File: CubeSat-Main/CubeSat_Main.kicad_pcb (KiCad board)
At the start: 2 copper layers, 92 x 92 mm, 22 parts, among them J1 Conn_01x03_Pin, J2 Conn_01x08_Socket, U1 STM32F411CEU6 - BlackPill, U2 LORA E220-900T22D, U3 BNO055, U4 GPS_NEO6M, U5 LM7805_TO220, U6 LM35-LP

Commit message: Mostly fine tuning the boards, also added capacitor for battery ADC
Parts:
- added C4: 0.1uF, Capacitor_THT:C_Disc_D8.0mm_W2.5mm_P5.00mm, F.Cu at (149.6, 98.3)
- added J3: Conn_01x03_Pin, Connector_PinHeader_2.54mm:PinHeader_1x03_P2.54mm_Vertical, F.Cu at (165.3, 97.0)
- C2, C3: footprint Capacitor_THT:C_Disc_D8.0mm_W5.0mm_P7.50mm -> Capacitor_THT:C_Disc_D8.0mm_W2.5mm_P5.00mm
- R6: value 100K -> 10K
- R7: value 47K -> 4.7K
- moved C3 6.77 mm to (120.6, 141.4), turned to 180 degrees
- moved C1 3.78 mm to (161.2, 93.2)
- moved R6 3.76 mm to (149.9, 91.1)
- moved R7 3.76 mm to (142.3, 94.8)
- moved U5 3.64 mm to (159.9, 98.1)
- moved C2 2.65 mm to (154.3, 103.8)
- moved U4 0.37 mm to (138.6, 70.6)
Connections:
- C3 pad 1: STM_3.3V -> GND
- C3 pad 2: GND -> VIN_5V2
- U1 pad 5V2: unconnected-(U1-5V-Pad5V2) -> VIN_5V2
- U2 pad 6: 5V_LDO -> 5V_E220
- U3 pad 1: STM_3.3V -> VIN_5V2
- U6 pad 1: 5V_LDO -> 5V_E220
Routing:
- net VIN_5V: track 44.8 -> 102.3 mm
- net STM_3.3V: track 77.8 -> 28.7 mm
- net 5V_E220: track 0.00 -> 45.2 mm
- net VIN_5V2: track 0.00 -> 41.7 mm
- net 5V_LDO: track 33.2 -> 20.8 mm
- net Vbat_ADC: track 8.87 -> 17.0 mm
- net GND: track 238.4 -> 240.7 mm
- net Net-(D2-K): track 4.14 -> 5.17 mm
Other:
- board text added: "-BNO055"
- board text added: "-GPS NEO6M"
- board text added: "-LoRa EBYTE 220"
- board text added: "-STM32F411CEU6"
- board text added: "BUCK"
- board text added: "LDO"
- board text added: "U2"

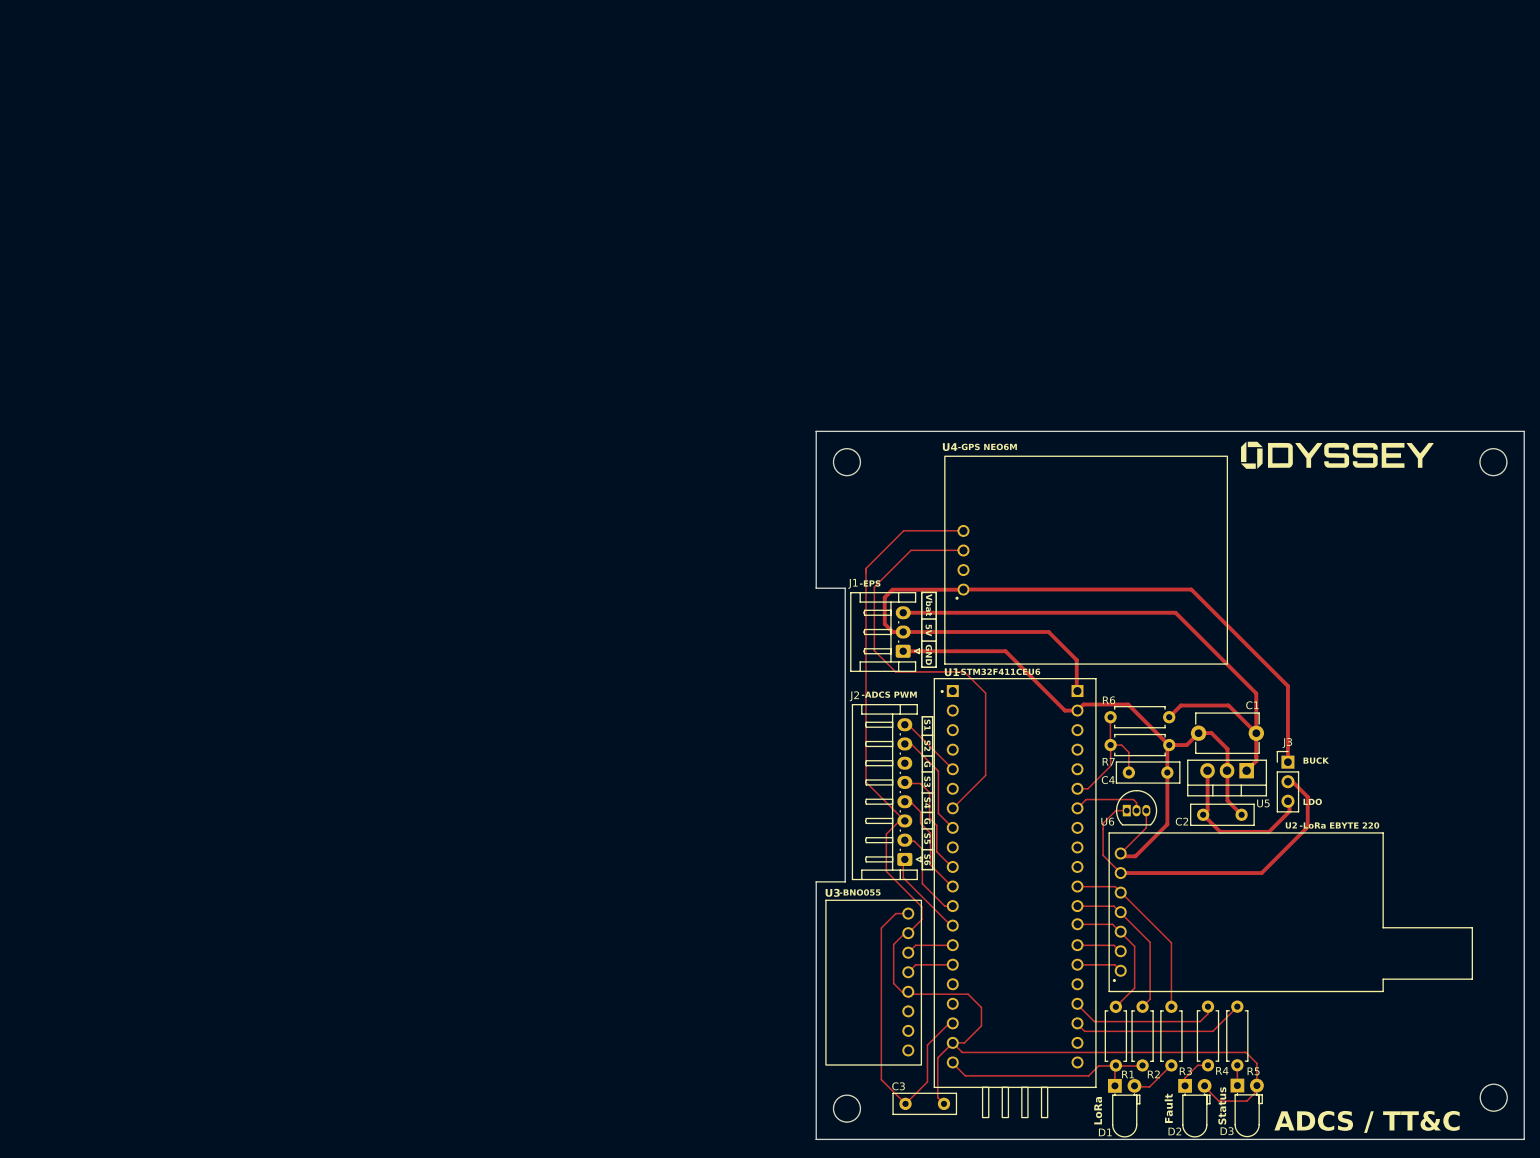
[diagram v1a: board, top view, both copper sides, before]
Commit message: Changing the size of all traces to fit the 1 mm requirement of the draft PCB
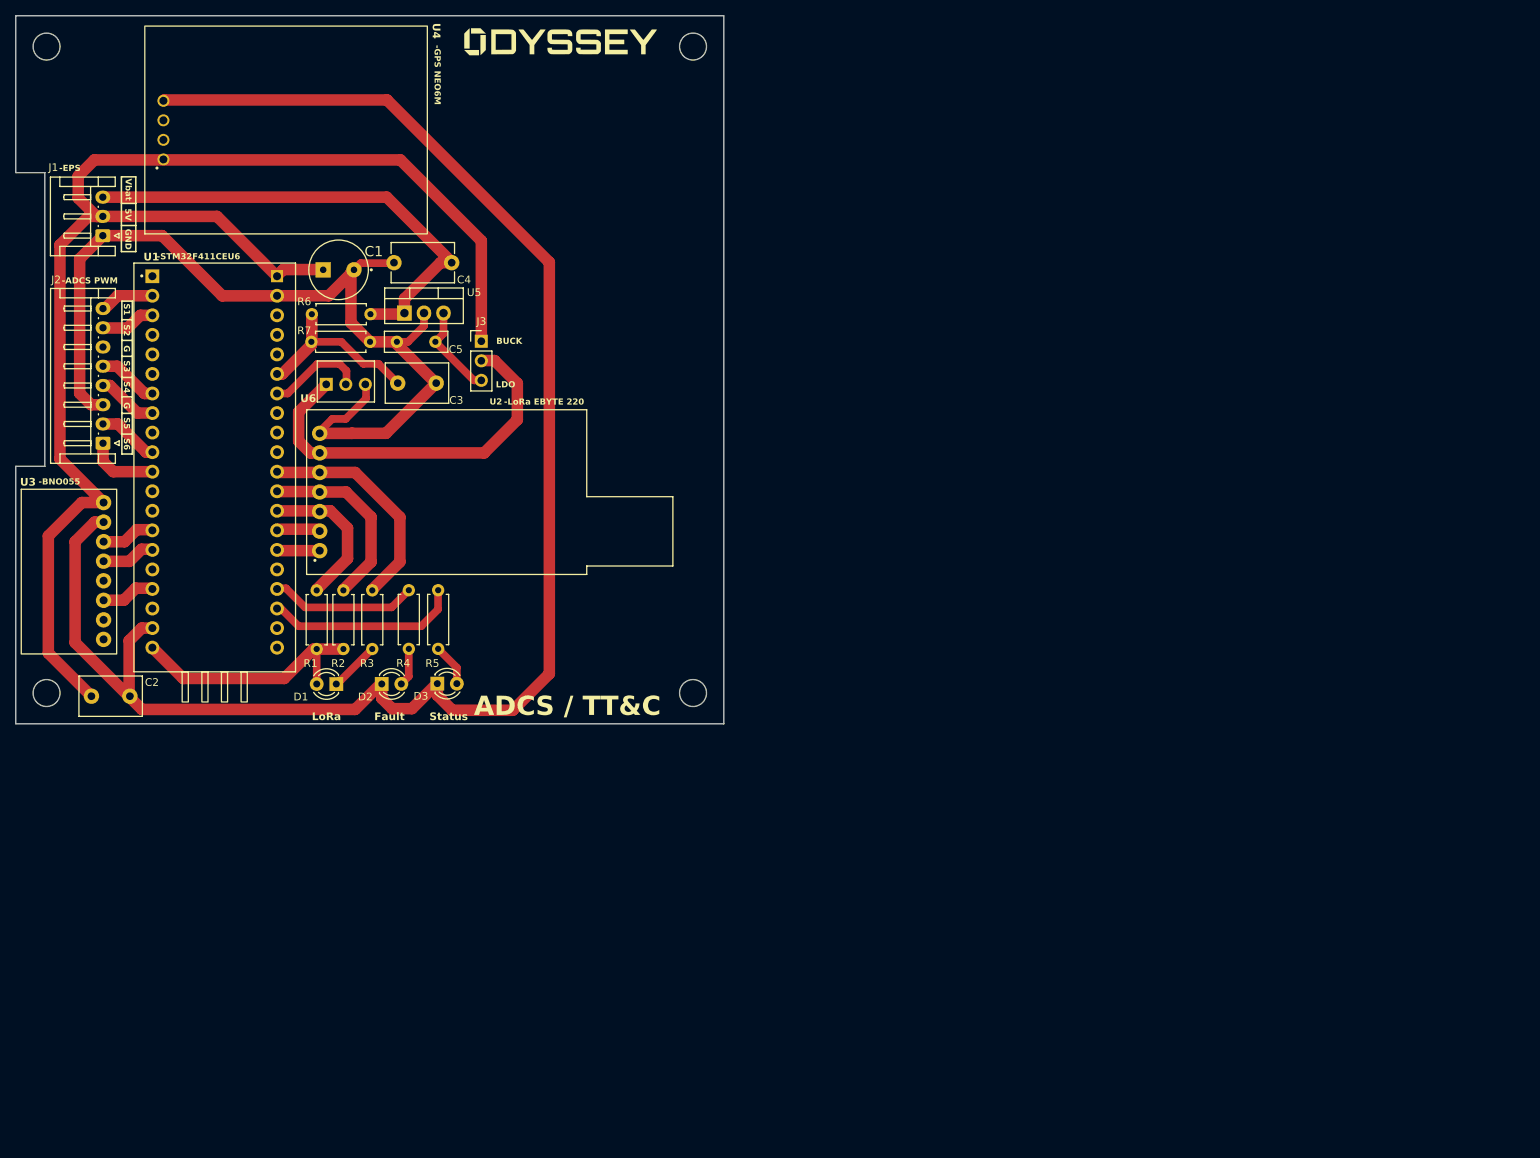
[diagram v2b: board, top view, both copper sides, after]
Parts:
- added C1: 22uF, Cubesat_Modules:Cap_Electrolytic, F.Cu at (41.9, 33.0)
- C2: renamed from C3; footprint Capacitor_THT:C_Disc_D8.0mm_W2.5mm_P5.00mm -> Capacitor_THT:C_Disc_D8.0mm_W5.0mm_P5.00mm
- C3: renamed from C4; footprint Capacitor_THT:C_Disc_D8.0mm_W2.5mm_P5.00mm -> Capacitor_THT:C_Disc_D8.0mm_W5.0mm_P5.00mm
- D1, D2, D3: footprint LED_THT:LED_D3.0mm_Horizontal_O1.27mm_Z2.0mm -> LED_THT:LED_D3.0mm
- R4: value 2.2K -> 1K
- R5: value 2.2k -> 1K
- U6: footprint Package_TO_SOT_THT:TO-92_Inline -> Cubesat_Modules:LM35DZ
- moved U5 124.5 mm to (50.5, 38.6), turned to 0 degrees
- moved C4 121.1 mm to (56.6, 32.1)
- moved C2 118.3 mm to (14.8, 88.4)
- moved J3 118.2 mm to (60.5, 42.3)
- moved U4 118.0 mm to (34.7, 14.7)
- moved U3 117.4 mm to (6.91, 72.2)
- moved J2 117.4 mm to (11.3, 55.5)
- moved U2 117.4 mm to (56.0, 61.9)
- moved J1 117.2 mm to (11.3, 28.6)
- moved U1 117.2 mm to (25.9, 58.3)
- moved C5 117.2 mm to (54.5, 42.4), turned to 180 degrees
- moved R1 117.1 mm to (39.1, 74.7)
- moved R2 117.1 mm to (42.6, 74.7)
- moved R3 117.1 mm to (46.3, 74.7)
- moved R4 117.1 mm to (51.1, 74.6)
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- renumbered C1 to C4, C2 to C5
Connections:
- C2 pad 2: VIN_5V2 -> VIN_5V
- D1 pad 1: STM_3.3V -> Net-(D1-K)
- D1 pad 2: Net-(D1-A) -> STM_3.3V
- D2 pad 1: Net-(D2-K) -> GND
- D2 pad 2: GND -> Net-(D2-A)
- D3 pad 1: Net-(D3-K) -> GND
- D3 pad 2: GND -> Net-(D3-A)
- R3 pad 2: Net-(D1-A) -> Net-(D1-K)
- R4 pad 2: Net-(D2-K) -> Net-(D2-A)
- R5 pad 2: Net-(D3-K) -> Net-(D3-A)
- U1 pad 26: unconnected-(U1-PB13-Pad26) -> M1_PWM1
- U1 pad 27: unconnected-(U1-PB14-Pad27) -> M1_PWM2
- U1 pad 29: M1_PWM1 -> unconnected-(U1-PA8-Pad29)
- U1 pad 31: GPS_TX -> M2_PWM1
- U1 pad 32: M1_PWM2 -> M2_PWM2
- U1 pad 38: M2_PWM1 -> M3_PWM1
- U1 pad 39: M2_PWM2 -> M3_PWM2
- U1 pad 40: M3_PWM1 -> unconnected-(U1-PB4-Pad40)
- U1 pad 41: M3_PWM2 -> unconnected-(U1-PB5-Pad41)
- U1 pad 46: unconnected-(U1-PB9-Pad46) -> BNO055_INT
- U1 pad 5V2: VIN_5V2 -> unconnected-(U1-5V-Pad5V2)
- U3 pad 1: VIN_5V2 -> VIN_5V
- U3 pad 5: GND -> unconnected-(U3-ADO-Pad5)
- U3 pad 6: unconnected-(U3-INT-Pad6) -> BNO055_INT
- U4 pad 3: GPS_TX -> unconnected-(U4-TX-Pad3)
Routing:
- net GND: track 240.7 -> 340.2 mm
- net VIN_5V: track 102.3 -> 185.0 mm
- net GPS_TX: track 55.0 -> 0.00 mm
- net VIN_5V2: track 41.7 -> 0.00 mm
- net Vbat_8.4V: track 74.4 -> 63.3 mm
- net 5V_LDO: track 20.8 -> 12.2 mm
- net M1_PWM2: track 14.1 -> 7.11 mm
- net Vbat_ADC: track 17.0 -> 23.9 mm
- net BNO055_INT: track 0.00 -> 6.79 mm
- net Net-(D1-K): track 0.00 -> 6.61 mm
- net M2_PWM2: track 14.1 -> 7.90 mm
- net Net-(D3-A): track 0.00 -> 6.24 mm
- net Net-(D1-A): track 5.96 -> 0.00 mm
- net M2_PWM1: track 14.8 -> 8.84 mm
- net E220_AUX: track 23.6 -> 29.4 mm
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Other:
- outline, holes or cut-outs redrawn

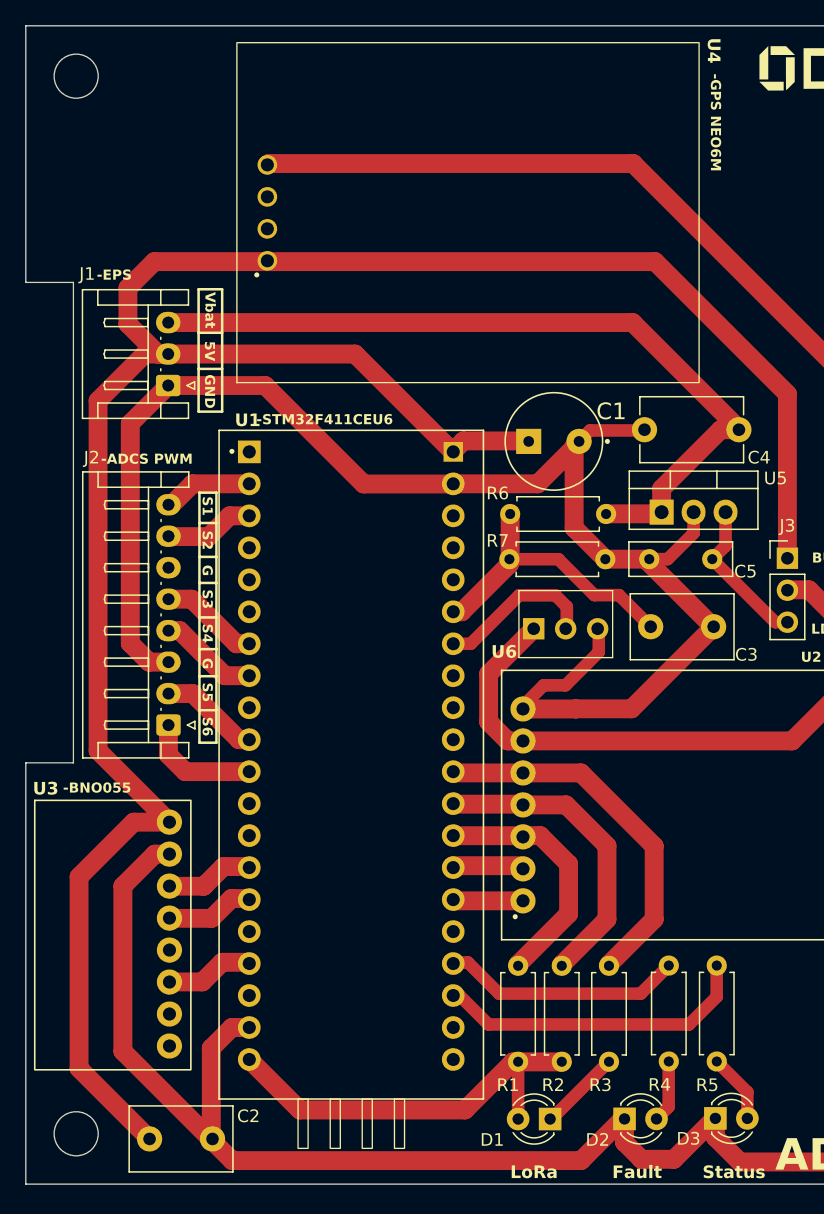
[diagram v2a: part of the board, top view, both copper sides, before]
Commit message: final version of the 3 PCBs, minor size changes for the protoypes
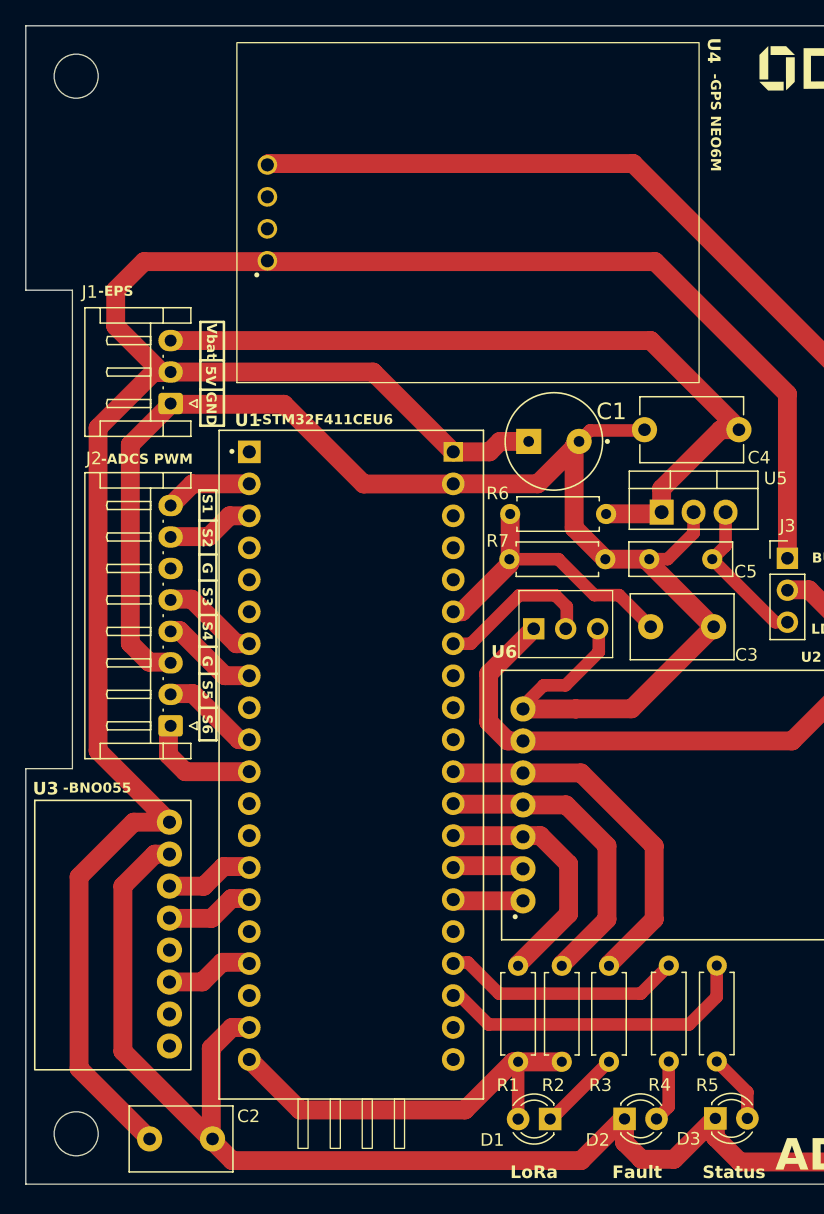
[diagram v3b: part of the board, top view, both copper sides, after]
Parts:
- moved J1 1.44 mm to (11.5, 30.0)
- moved J2 0.18 mm to (11.5, 55.6)
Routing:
- net GND: track 340.2 -> 337.9 mm
- net Vbat_8.4V: track 63.3 -> 62.7 mm
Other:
- outline, holes or cut-outs redrawn

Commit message: final changes
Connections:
- U1 pad 38: M3_PWM1 -> unconnected-(U1-PA15-Pad38)
- U1 pad 39: M3_PWM2 -> unconnected-(U1-PB3-Pad39)
- U1 pad 40: unconnected-(U1-PB4-Pad40) -> M3_PWM1
- U1 pad 41: unconnected-(U1-PB5-Pad41) -> M3_PWM2
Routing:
- net M3_PWM1: track 7.96 -> 13.0 mm
- net M3_PWM2: track 9.47 -> 12.1 mm
- net GND: track 337.9 -> 338.5 mm

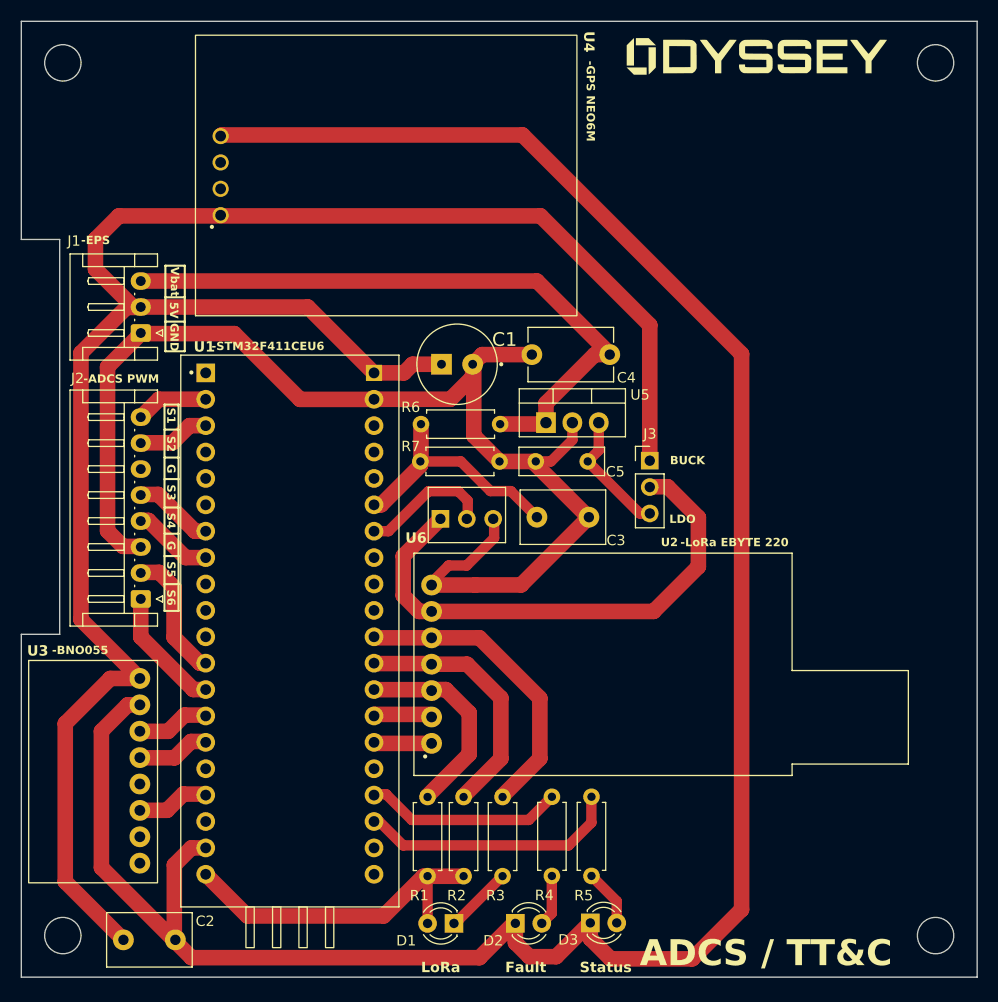
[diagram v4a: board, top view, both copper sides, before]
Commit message: add new drill format
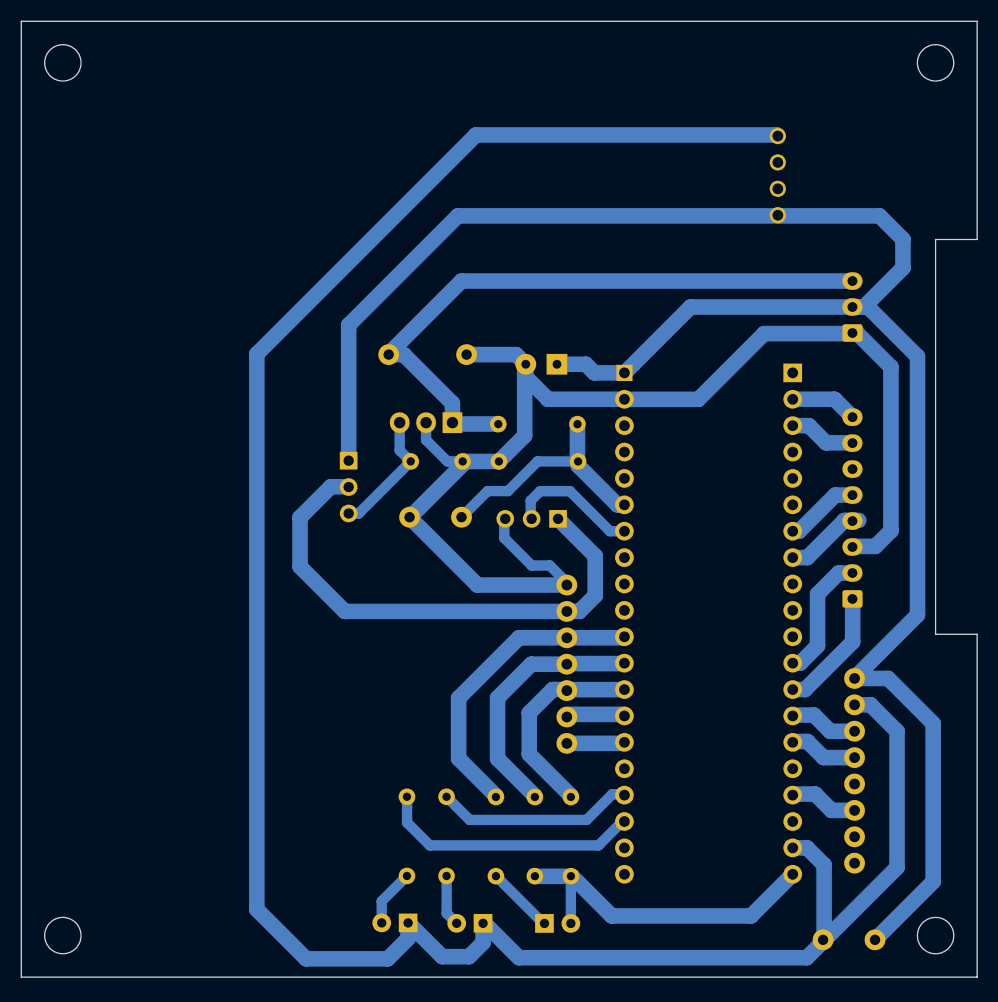
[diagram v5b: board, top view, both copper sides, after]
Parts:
- C1, C2, C3, C4, C5, D1, D2, D3, G***, J1, J2, J3, R1, R2, R3, R4, R5, R6, R7, U1, U2, U3, U4, U5, U6: moved to B.Cu
- moved U3 77.8 mm to (84.7, 72.2), turned to 180 degrees
- moved J1 68.5 mm to (80.0, 30.0)
- moved J2 68.5 mm to (80.0, 55.6)
- moved C2 62.3 mm to (77.2, 88.4), turned to 0 degrees
- moved G*** 48.5 mm to (22.4, 3.38), turned to 180 degrees
- moved U1 40.3 mm to (66.2, 58.3), turned to 180 degrees
- moved J3 29.0 mm to (31.5, 42.3), turned to 180 degrees
- moved U4 22.7 mm to (57.3, 14.7)
- moved C4 21.3 mm to (35.4, 32.1), turned to 0 degrees
- moved U2 20.0 mm to (36.0, 61.9)
- moved R5 17.8 mm to (37.1, 74.6)
- moved D3 17.5 mm to (37.2, 86.8), turned to 180 degrees
- moved C3 17.3 mm to (37.4, 47.7), turned to 0 degrees
- moved C5 17.0 mm to (37.5, 42.4), turned to 0 degrees
- moved R7 15.2 mm to (53.6, 42.4), turned to 180 degrees
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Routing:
- net M2_PWM1: track 8.81 -> 7.22 mm
- net GND: track 338.5 -> 339.6 mm
- net Vbat_8.4V: track 62.7 -> 62.0 mm
- net M1_PWM2: track 7.11 -> 6.45 mm
- net M1_PWM1: track 7.17 -> 6.52 mm
- net M3_PWM1: track 13.0 -> 12.4 mm
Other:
- outline, holes or cut-outs redrawn
